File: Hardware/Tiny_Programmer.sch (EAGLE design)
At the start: 31 parts, among them Q1 16MHz, U1 ATTINY84, X1 USB-A-H

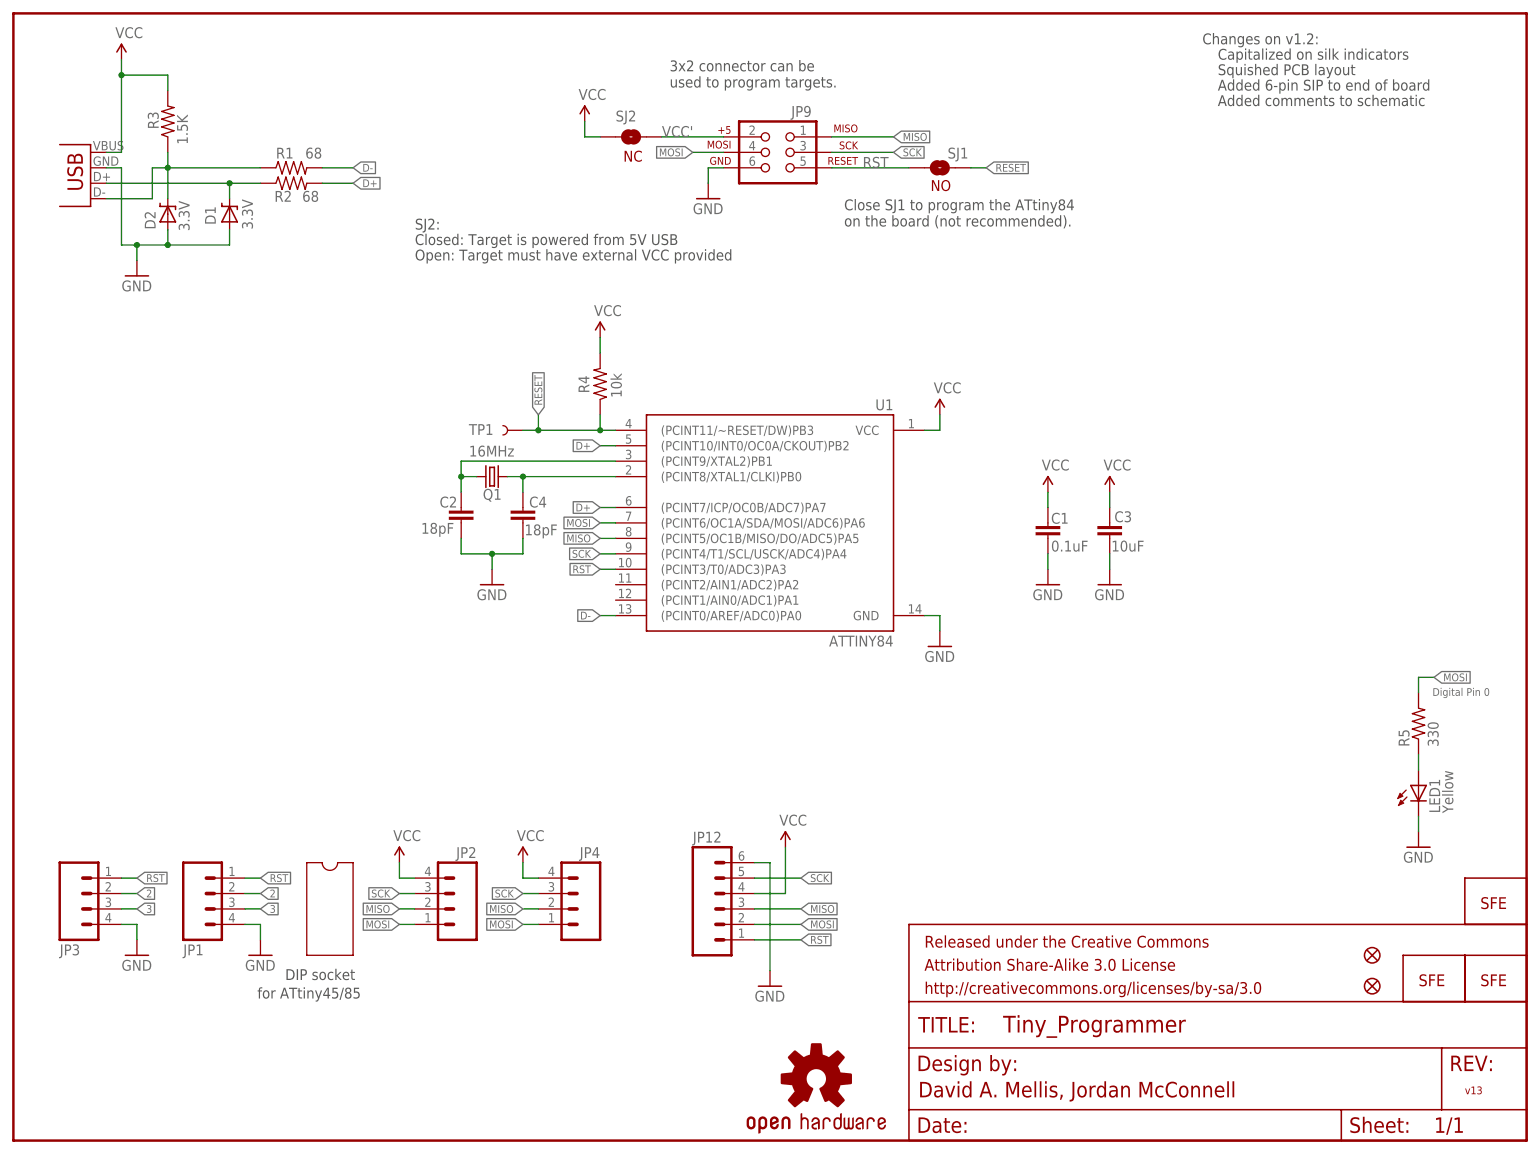
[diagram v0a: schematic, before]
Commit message: Removed ATTINY85 socket & headers.  Replaced USB A plug with USB Micro B socket.  Shrinkified board layout.  Added shrouded 6-pin ISP header.
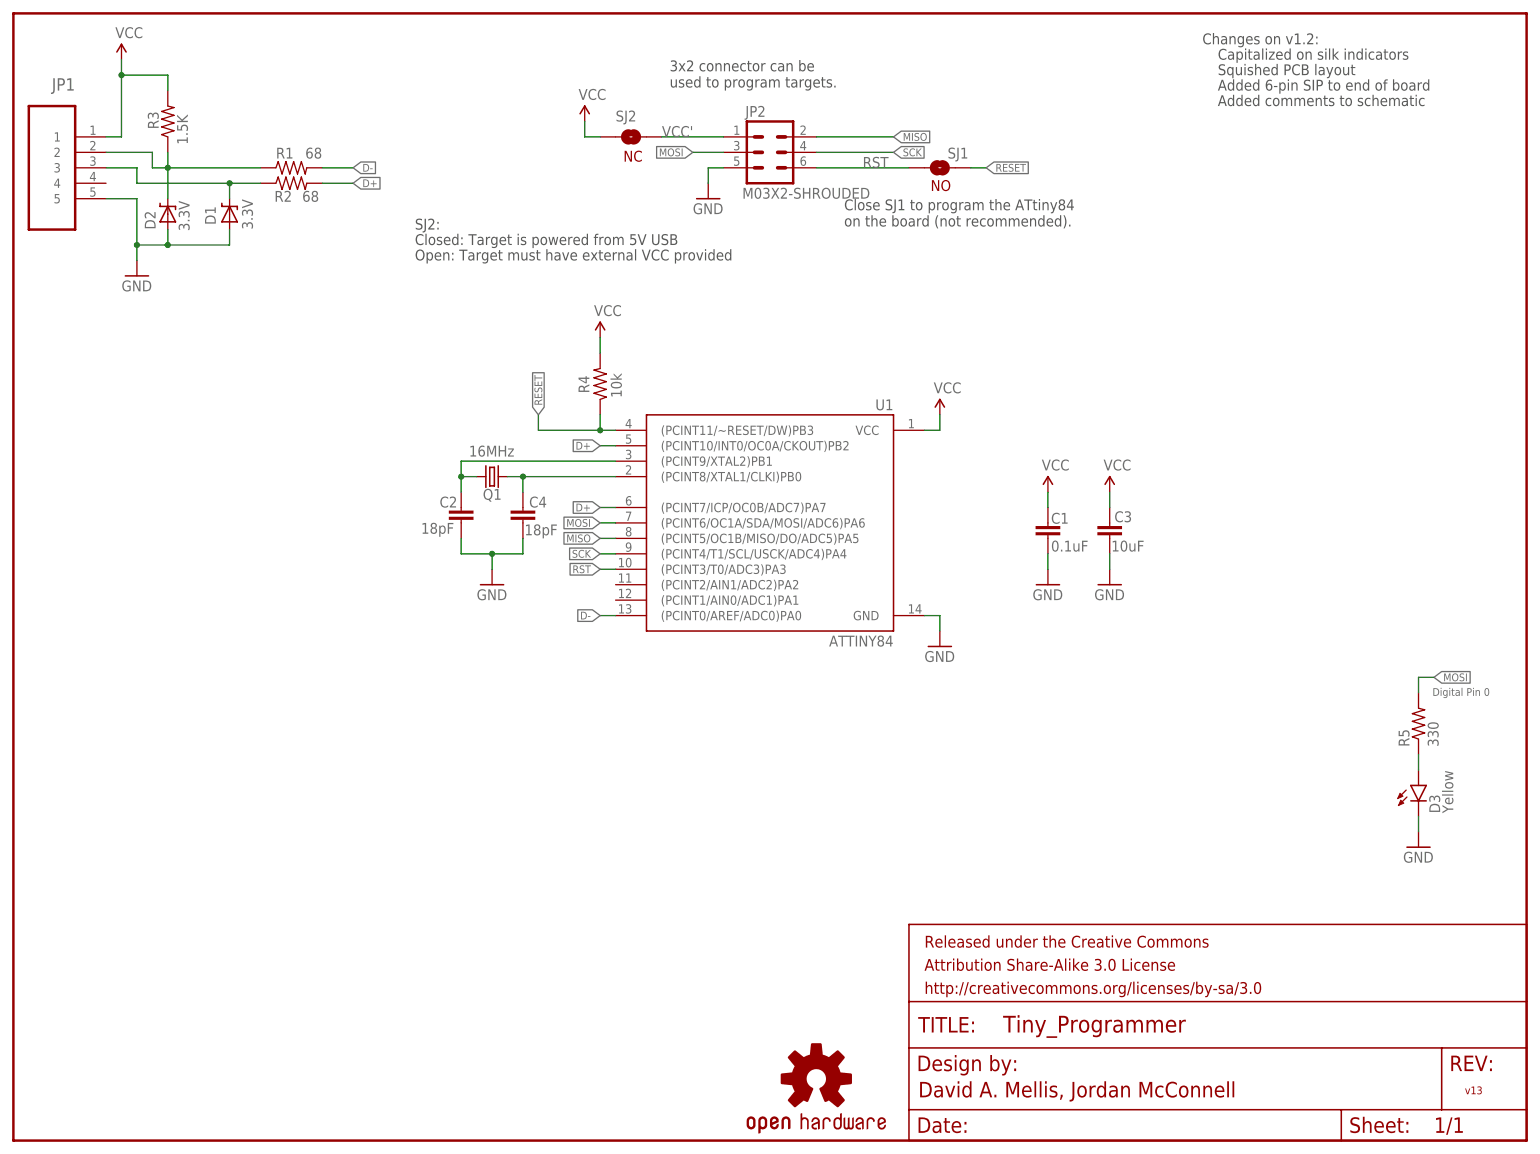
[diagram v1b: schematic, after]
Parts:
- removed JP11, JP6: LOGO-SFESK, SparkFun-Aesthetics:LOGO-SFESK
- removed JP12: (no value), SparkFun-Connectors:M06SIP
- removed JP3, JP4: (no value), SparkFun-Connectors:M04SMD_STRAIGHT_COMBO
- removed JP5: LOGO-SFENW2, SparkFun-Aesthetics:LOGO-SFENW2
- removed JP7, JP8: FIDUCIALUFIDUCIAL, SparkFun:FIDUCIALUFIDUCIAL
- removed JP9: AVR_SPI_PRG_6PTH, SparkFun-Connectors:AVR_SPI_PRG_6PTH
- removed TP1: TEST-POINT3, SparkFun-Passives:TEST-POINT3
- removed X1: USB-A-H, SparkFun-Connectors:USB-A-H
- C1, C2, C3, C4: device SparkFun-Passives:CAP0402-CAP -> SparkFun-Capacitors:CAP0603-CAP
- JP1: device SparkFun-Connectors:M04PTH -> Molex-47346-0001:47346-0001
- JP2: value (none) -> M03X2-SHROUDED; device SparkFun-Connectors:M04PTH -> Darryl:M03X2-SHROUDED
- R1, R2, R3, R4, R5: device SparkFun-Passives:RESISTOR0402-RES -> SparkFun-Resistors:RESISTOR0603
- renumbered LED1 to D3
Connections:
- removed net 2: JP1.2, JP3.2
- removed net 3: JP1.3, JP3.3
- removed net N$1: D2.C, R1.1, R3.1, X1.D+
- removed net N$2: D1.C, R2.1, X1.D-
- new net USBDM: D2.C, JP1.2, R1.1, R3.1
- new net USBSP: D1.C, JP1.3, R2.1
- net GND: now also JP1.5, JP2.5; no longer JP1.4, JP12.6, JP3.4, JP9.6, X1.VBUS
- net MISO: no longer JP12.3, JP4.2, JP9.1
- net MOSI: now also JP2.3; no longer JP12.2, JP2.1, JP4.1, JP9.4
- net RESET: no longer TP1.1
- net RST: now also JP2.6; no longer JP1.1, JP12.1, JP3.1, JP9.5
- net SCK: now also JP2.4; no longer JP12.5, JP2.3, JP4.3, JP9.3
- net VCC: now also JP1.1; no longer JP12.4, JP2.4, JP4.4, X1.GND
- net VCC': now also JP2.1; no longer JP9.2
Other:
- note removed: "DIP socket"
- note removed: "for ATtiny45/85"
